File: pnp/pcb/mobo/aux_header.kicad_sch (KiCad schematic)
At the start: 1 part, among them J20 AUX

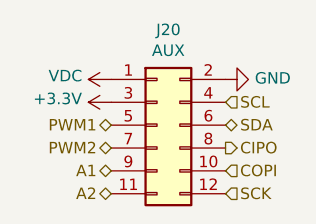
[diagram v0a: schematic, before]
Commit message: Mobo V4A Redesign
Some EMC improvements to schematics.
Reassigned MCU Pins for HW-PWM support.
Changes are still marked with text in the schematics.
Complete PCB Layout reworked
Status: Needs to be verified, and cleaned up a little, but DRC is running green.
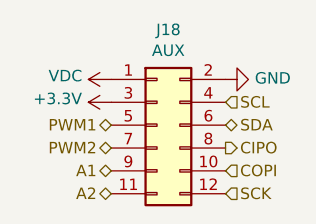
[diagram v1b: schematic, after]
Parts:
- renumbered J20 to J18
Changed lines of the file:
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@@
   (title_block
     (title "LumenPnP Motherboard")
-    (date "2022-03-29")
+    (date "2022-09-09")
+    (rev "004A")
     (company "Opulo")
+    (comment 1 "Reengineered by Magpie")
   )
   (hierarchical_label "PWM1" (shape bidirectional) (at 138.43 97.155 180)
@@
     (effects (font (size 1.27 1.27)) (justify left))
   )
-  (symbol (lib_id "power:GND") (at 151.13 92.075 90)
+  (symbol (lib_id "power:GND") (at 151.13 92.075 90) (unit 1)
     (in_bom yes) (on_board yes)
-    (property "Reference" "#PWR0238" (id 0) (at 157.48 92.075 0)
+    (property "Reference" "#PWR0232" (id 0) (at 157.48 92.075 0)
       (effects (font (size 1.27 1.27)) hide)
     )
@@
     (pin "1")
   )
-  (symbol (lib_id "power:VDC") (at 138.43 92.075 90)
+  (symbol (lib_id "power:VDC") (at 138.43 92.075 90) (unit 1)
     (in_bom yes) (on_board yes)
-    (property "Reference" "#PWR0236" (id 0) (at 140.97 92.075 0)
+    (property "Reference" "#PWR0230" (id 0) (at 140.97 92.075 0)
       (effects (font (size 1.27 1.27)) hide)
     )
@@
     (pin "1")
   )
-  (symbol (lib_id "Connector_Generic:Conn_02x06_Odd_Even") (at 143.51 97.155 0)
+  (symbol (lib_id "Connector_Generic:Conn_02x06_Odd_Even") (at 143.51 97.155 0) (unit 1)
     (in_bom yes) (on_board yes)
-    (property "Reference" "J20" (id 0) (at 144.78 86.5632 0))
+    (property "Reference" "J18" (id 0) (at 144.78 86.5632 0))
     (property "Value" "AUX" (id 1) (at 144.78 88.8746 0))
     (property "Footprint" "Connector_IDC:IDC-Header_2x06_P2.54mm_Vertical" (id 2) (at 143.51 97.155 0)
@@
     (pin "9")
   )
-  (symbol (lib_id "power:+3.3V") (at 138.43 94.615 90)
+  (symbol (lib_id "power:+3.3V") (at 138.43 94.615 90) (unit 1)
     (in_bom yes) (on_board yes)
-    (property "Reference" "#PWR0237" (id 0) (at 142.24 94.615 0)
+    (property "Reference" "#PWR0231" (id 0) (at 142.24 94.615 0)
       (effects (font (size 1.27 1.27)) hide)
     )

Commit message: Redesign finished
Completed Board redesign and adding more EMC improvements.
Changed all the part numbers to have a Mouser orderable design (except the JST connectors)
All outputs generated
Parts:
- J18: LCSC C9136 -> (none); Mouser (none) -> 538-87834-1211
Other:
- company: Opulo -> Opulo.io
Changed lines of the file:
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@@
   (title_block
     (title "LumenPnP Motherboard")
-    (date "2022-09-09")
-    (rev "004A")
-    (company "Opulo")
+    (date "2022-10-06")
+    (rev "04A")
+    (company "Opulo.io")
     (comment 1 "Reengineered by Magpie")
   )
@@
       (effects (font (size 1.27 1.27)) hide)
     )
-    (property "LCSC" "C9136" (id 4) (at 143.51 97.155 0)
+    (property "LCSC" "" (id 4) (at 143.51 97.155 0)
       (effects (font (size 1.27 1.27)) hide)
     )
+    (property "Mouser" "538-87834-1211" (id 5) (at 143.51 97.155 0)
+      (effects (font (size 1.27 1.27)) hide)
+    )
